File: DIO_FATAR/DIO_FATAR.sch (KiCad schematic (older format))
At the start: 8 parts, among them J1 in, J2 thru

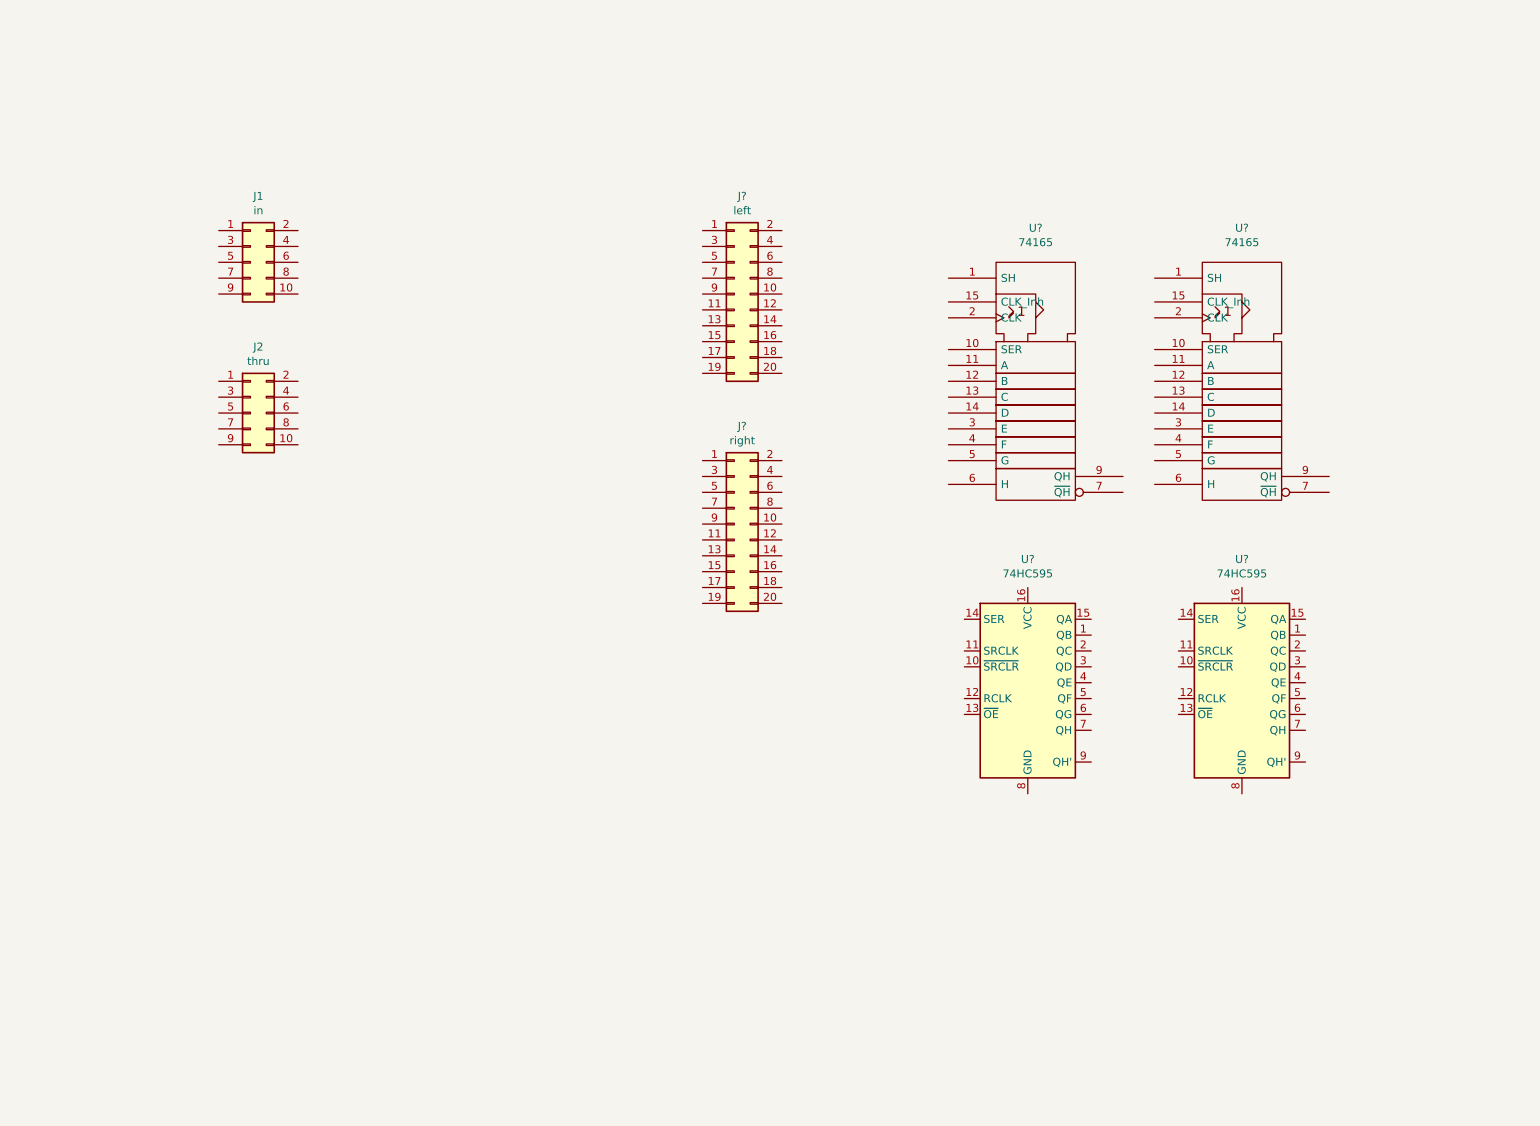
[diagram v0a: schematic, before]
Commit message: DIO_FATAR: schematic mostly done
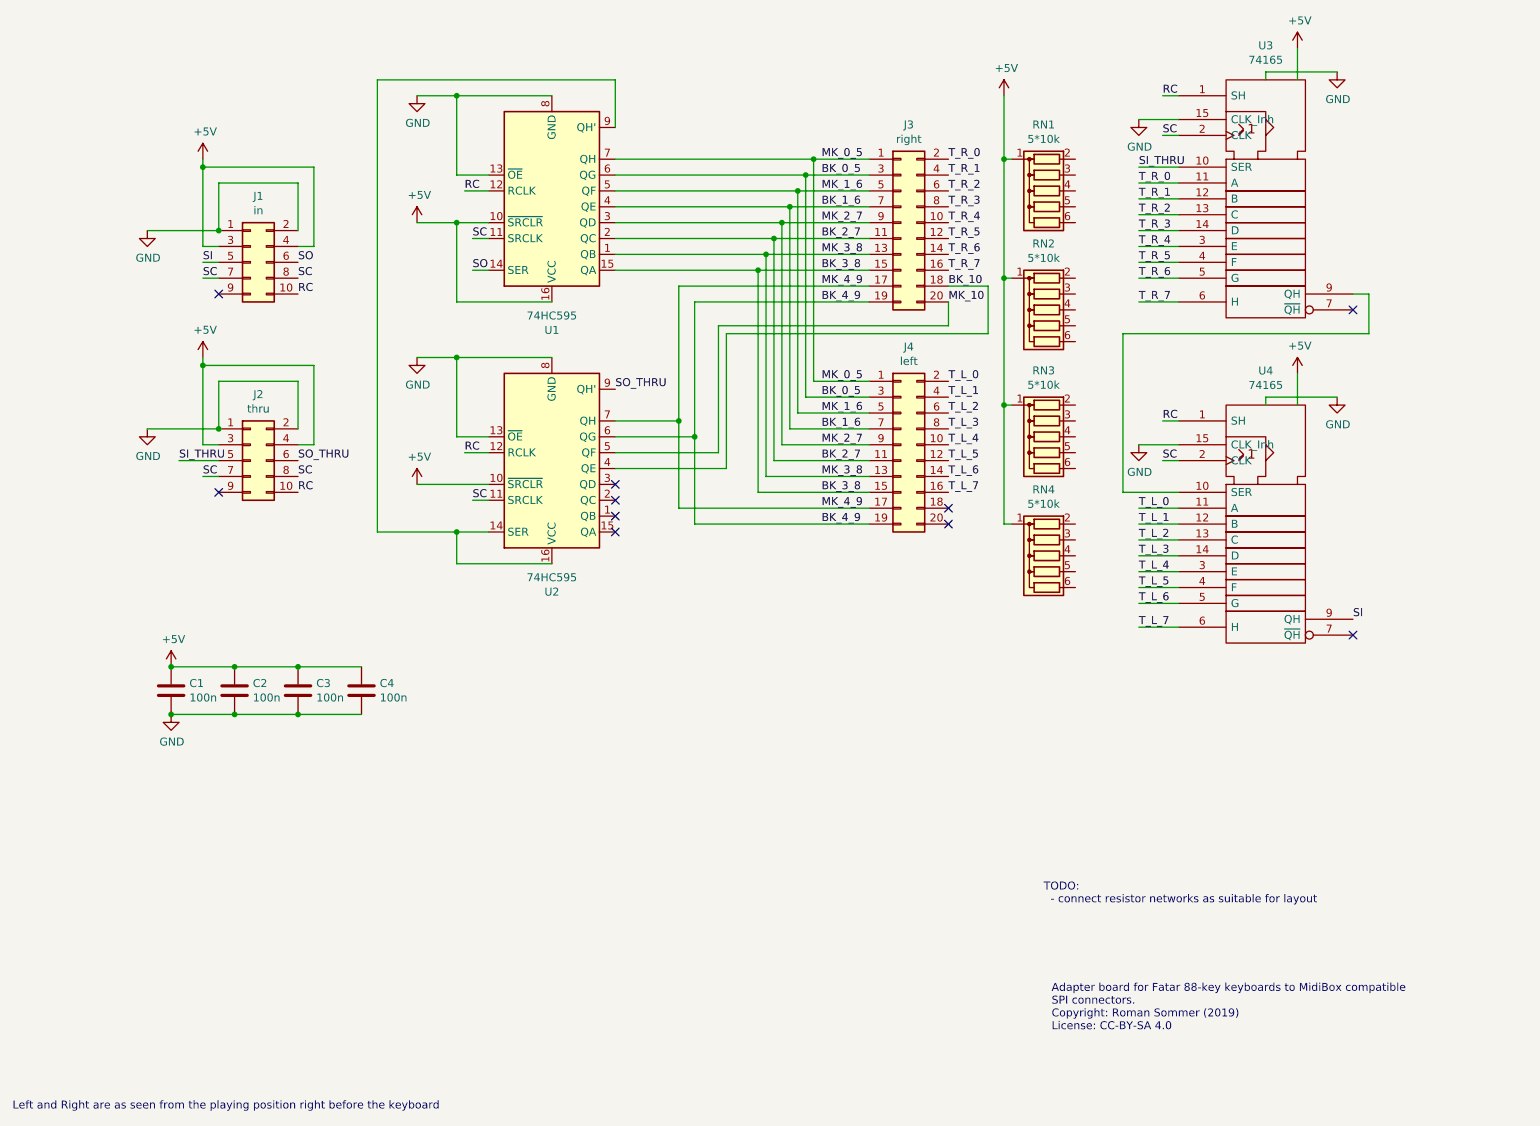
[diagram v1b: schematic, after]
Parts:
- added C1, C2, C3, C4: 100n, symbol Device:C
- added RN1, RN2, RN3, RN4: 5*10k, Resistor_THT:R_Array_SIP6, symbol Device:R_Network05
- gave numbers to parts that had none: 6
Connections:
- net VCC is gone; now on net +5V: U3.16 (VCC), U4.16 (VCC)
- net GND: now also J1.1 (Pin_1), J1.2 (Pin_2), J2.1 (Pin_1), J2.2 (Pin_2), U1.13 (~OE), U1.8 (GND), U2.13 (~OE), U2.8 (GND), U3.15 (CLK_Inh), U4.15 (CLK_Inh), C1.2, C2.2, C3.2, C4.2
- net RC: now reaches J1.10 (Pin_10)
- net RC: now also J2.10 (Pin_10), U1.12 (RCLK), U2.12 (RCLK), U3.1 (SH), U4.1 (SH)
- net +5V: now reaches J1.3 (Pin_3)
- net +5V: now also J1.4 (Pin_4), J2.3 (Pin_3), J2.4 (Pin_4), U1.10 (~SRCLR), U1.16 (VCC), U2.10 (~SRCLR), C1.1, C2.1, C3.1, C4.1, RN1.1 (common), RN2.1 (common), RN3.1 (common), RN4.1 (common)
- net SI: now reaches J1.5 (Pin_5)
- net SI: now also U4.9 (QH)
- net SO: now reaches J1.6 (Pin_6)
- net SO: now also U1.14 (SER)
- net SC: now reaches J1.7 (Pin_7)
- net SC: now also J1.8 (Pin_8), J2.7 (Pin_7), J2.8 (Pin_8), U1.11 (SRCLK), U2.11 (SRCLK), U3.2 (CLK), U4.2 (CLK)
- net MK_0_5: now reaches J4.1 (Pin_1)
- net MK_0_5: now also J3.1 (Pin_1), U1.7 (QH)
- net T_L_4: now reaches J4.10 (Pin_10)
- net T_L_4: now also U4.3 (E)
- net BK_2_7: now reaches J4.11 (Pin_11)
- net BK_2_7: now also J3.11 (Pin_11), U1.2 (QC)
- net T_L_5: now reaches J4.12 (Pin_12)
- net T_L_5: now also U4.4 (F)
- net MK_3_8: now reaches J4.13 (Pin_13)
- net MK_3_8: now also J3.13 (Pin_13), U1.1 (QB)
- net T_L_6: now reaches J4.14 (Pin_14)
- net T_L_6: now also U4.5 (G)
- net BK_3_8: now reaches J4.15 (Pin_15)
- net BK_3_8: now also J3.15 (Pin_15), U1.15 (QA)
- net T_L_7: now reaches J4.16 (Pin_16)
- net T_L_7: now also U4.6 (H)
- net MK_4_9: now reaches J4.17 (Pin_17)
- net MK_4_9: now also J3.17 (Pin_17), U2.7 (QH)
- net BK_4_9: now reaches J4.19 (Pin_19)
- net BK_4_9: now also J3.19 (Pin_19), U2.6 (QG)
- net T_L_0: now reaches J4.2 (Pin_2)
- net T_L_0: now also U4.11 (A)
- net BK_0_5: now reaches J4.3 (Pin_3)
- net BK_0_5: now also J3.3 (Pin_3), U1.6 (QG)
- net T_L_1: now reaches J4.4 (Pin_4)
- net T_L_1: now also U4.12 (B)
- net MK_1_6: now reaches J4.5 (Pin_5)
- net MK_1_6: now also J3.5 (Pin_5), U1.5 (QF)
- net T_L_2: now reaches J4.6 (Pin_6)
- net T_L_2: now also U4.13 (C)
- net BK_1_6: now reaches J4.7 (Pin_7)
- net BK_1_6: now also J3.7 (Pin_7), U1.4 (QE)
- net T_L_3: now reaches J4.8 (Pin_8)
- net T_L_3: now also U4.14 (D)
- net MK_2_7: now reaches J4.9 (Pin_9)
- net MK_2_7: now also J3.9 (Pin_9), U1.3 (QD)
- net T_R_4: now reaches J3.10 (Pin_10)
- net T_R_4: now also U3.3 (E)
- net T_R_5: now reaches J3.12 (Pin_12)
- net T_R_5: now also U3.4 (F)
- net T_R_6: now reaches J3.14 (Pin_14)
- net T_R_6: now also U3.5 (G)
- net T_R_7: now reaches J3.16 (Pin_16)
- net T_R_7: now also U3.6 (H)
- net BK_10: now reaches J3.18 (Pin_18)
- net BK_10: now also U2.4 (QE)
- net T_R_0: now reaches J3.2 (Pin_2)
- net T_R_0: now also U3.11 (A)
- net MK_10: now reaches J3.20 (Pin_20)
- net MK_10: now also U2.5 (QF)
- net T_R_1: now reaches J3.4 (Pin_4)
- net T_R_1: now also U3.12 (B)
- net T_R_2: now reaches J3.6 (Pin_6)
- net T_R_2: now also U3.13 (C)
- net T_R_3: now reaches J3.8 (Pin_8)
- net T_R_3: now also U3.14 (D)
- net SI_THRU: now reaches J2.5 (Pin_5)
- net SI_THRU: now also U3.10 (SER)
- net SO_THRU: now reaches J2.6 (Pin_6)
- net SO_THRU: now also U2.9 (QH')
- net at U4.10 (SER): now also U3.9 (QH)
- net at U1.9 (QH'): now also U2.14 (SER), U2.16 (VCC)
- no-connect marks 0 -> 10
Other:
- note added: "Adapter board for Fatar 88-key keyboards to MidiBox compatible\nSPI connectors.\nCopyright: Roman Sommer (2019)\nLicense: CC-BY-SA 4.0"
- note added: "Left and Right are as seen from the playing position right before the keyboard"
- note added: "TODO:\n - connect resistor networks as suitable for layout\n"
- moved on the sheet: J2, J3, J4, U1, U2, U3, U4

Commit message: DIO_FATAR: add footprint annotations
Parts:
- C1, C2, C3, C4: footprint (none) -> Capacitor_THT:C_Disc_D5.1mm_W3.2mm_P5.00mm
- J1, J2: footprint (none) -> Connector_IDC:IDC-Header_2x05_P2.54mm_Vertical
- J3, J4: footprint (none) -> Connector_IDC:IDC-Header_2x10_P2.54mm_Vertical
- U1, U2, U3, U4: footprint (none) -> Package_DIP:DIP-16_W7.62mm_Socket_LongPads
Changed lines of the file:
@@
 F 0 "J1" H 2200 2567 50  0000 C CNN
 F 1 "in" H 2200 2476 50  0000 C CNN
-F 2 "" H 2150 2150 50  0001 C CNN
+F 2 "Connector_IDC:IDC-Header_2x05_P2.54mm_Vertical" H 2150 2150 50  0001 C CNN
 F 3 "~" H 2150 2150 50  0001 C CNN
 	1    2150 2150
@@
 F 0 "J4" H 6300 3917 50  0000 C CNN
 F 1 "left" H 6300 3826 50  0000 C CNN
-F 2 "" H 6250 3300 50  0001 C CNN
+F 2 "Connector_IDC:IDC-Header_2x10_P2.54mm_Vertical" H 6250 3300 50  0001 C CNN
 F 3 "~" H 6250 3300 50  0001 C CNN
 	1    6250 3300
@@
 F 0 "J3" H 6300 2517 50  0000 C CNN
 F 1 "right" H 6300 2426 50  0000 C CNN
-F 2 "" H 6250 1900 50  0001 C CNN
+F 2 "Connector_IDC:IDC-Header_2x10_P2.54mm_Vertical" H 6250 1900 50  0001 C CNN
 F 3 "~" H 6250 1900 50  0001 C CNN
 	1    6250 1900
@@
 F 0 "J2" H 2200 3817 50  0000 C CNN
 F 1 "thru" H 2200 3726 50  0000 C CNN
-F 2 "" H 2150 3400 50  0001 C CNN
+F 2 "Connector_IDC:IDC-Header_2x05_P2.54mm_Vertical" H 2150 3400 50  0001 C CNN
 F 3 "~" H 2150 3400 50  0001 C CNN
 	1    2150 3400
@@
 F 0 "U4" H 8550 4366 50  0000 C CNN
 F 1 "74165" H 8550 4275 50  0000 C CNN
-F 2 "" H 8550 3600 50  0001 C CNN
+F 2 "Package_DIP:DIP-16_W7.62mm_Socket_LongPads" H 8550 3600 50  0001 C CNN
 F 3 "" H 8550 3600 50  0001 C CNN
 	1    8550 3600
@@
 F 0 "U3" H 8550 2316 50  0000 C CNN
 F 1 "74165" H 8550 2225 50  0000 C CNN
-F 2 "" H 8550 1550 50  0001 C CNN
+F 2 "Package_DIP:DIP-16_W7.62mm_Socket_LongPads" H 8550 1550 50  0001 C CNN
 F 3 "" H 8550 1550 50  0001 C CNN
 	1    8550 1550
@@
 F 0 "U1" H 4050 2578 50  0000 C CNN
 F 1 "74HC595" H 4050 2487 50  0000 C CNN
-F 2 "" H 4050 1800 50  0001 C CNN
+F 2 "Package_DIP:DIP-16_W7.62mm_Socket_LongPads" H 4050 1800 50  0001 C CNN
 F 3 "http://www.ti.com/lit/ds/symlink/sn74hc595.pdf" H 4050 1800 50  0001 C CNN
 	1    4050 1800
@@
 F 0 "U2" H 4050 4228 50  0000 C CNN
 F 1 "74HC595" H 4050 4137 50  0000 C CNN
-F 2 "" H 4050 3450 50  0001 C CNN
+F 2 "Package_DIP:DIP-16_W7.62mm_Socket_LongPads" H 4050 3450 50  0001 C CNN
 F 3 "http://www.ti.com/lit/ds/symlink/sn74hc595.pdf" H 4050 3450 50  0001 C CNN
 	1    4050 3450
@@
 F 0 "C1" H 1765 4896 50  0000 L CNN
 F 1 "100n" H 1765 4805 50  0000 L CNN
-F 2 "" H 1688 4700 50  0001 C CNN
+F 2 "Capacitor_THT:C_Disc_D5.1mm_W3.2mm_P5.00mm" H 1688 4700 50  0001 C CNN
 F 3 "~" H 1650 4850 50  0001 C CNN
 	1    1650 4850
@@
 F 0 "C2" H 2165 4896 50  0000 L CNN
 F 1 "100n" H 2165 4805 50  0000 L CNN
-F 2 "" H 2088 4700 50  0001 C CNN
+F 2 "Capacitor_THT:C_Disc_D5.1mm_W3.2mm_P5.00mm" H 2088 4700 50  0001 C CNN
 F 3 "~" H 2050 4850 50  0001 C CNN
 	1    2050 4850
@@
 F 0 "C3" H 2565 4896 50  0000 L CNN
 F 1 "100n" H 2565 4805 50  0000 L CNN
-F 2 "" H 2488 4700 50  0001 C CNN
+F 2 "Capacitor_THT:C_Disc_D5.1mm_W3.2mm_P5.00mm" H 2488 4700 50  0001 C CNN
 F 3 "~" H 2450 4850 50  0001 C CNN
 	1    2450 4850
@@
 F 0 "C4" H 2965 4896 50  0000 L CNN
 F 1 "100n" H 2965 4805 50  0000 L CNN
-F 2 "" H 2888 4700 50  0001 C CNN
+F 2 "Capacitor_THT:C_Disc_D5.1mm_W3.2mm_P5.00mm" H 2888 4700 50  0001 C CNN
 F 3 "~" H 2850 4850 50  0001 C CNN
 	1    2850 4850

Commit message: DIO_FATAR: use socketless footprint for DIP packages, add netlist
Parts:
- U1, U2, U3, U4: footprint Package_DIP:DIP-16_W7.62mm_Socket_LongPads -> Package_DIP:DIP-16_W7.62mm_LongPads
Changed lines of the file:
@@
 F 0 "U4" H 8550 4366 50  0000 C CNN
 F 1 "74165" H 8550 4275 50  0000 C CNN
-F 2 "Package_DIP:DIP-16_W7.62mm_Socket_LongPads" H 8550 3600 50  0001 C CNN
+F 2 "Package_DIP:DIP-16_W7.62mm_LongPads" H 8550 3600 50  0001 C CNN
 F 3 "" H 8550 3600 50  0001 C CNN
 	1    8550 3600
@@
 F 0 "U3" H 8550 2316 50  0000 C CNN
 F 1 "74165" H 8550 2225 50  0000 C CNN
-F 2 "Package_DIP:DIP-16_W7.62mm_Socket_LongPads" H 8550 1550 50  0001 C CNN
+F 2 "Package_DIP:DIP-16_W7.62mm_LongPads" H 8550 1550 50  0001 C CNN
 F 3 "" H 8550 1550 50  0001 C CNN
 	1    8550 1550
@@
 F 0 "U1" H 4050 2578 50  0000 C CNN
 F 1 "74HC595" H 4050 2487 50  0000 C CNN
-F 2 "Package_DIP:DIP-16_W7.62mm_Socket_LongPads" H 4050 1800 50  0001 C CNN
+F 2 "Package_DIP:DIP-16_W7.62mm_LongPads" H 4050 1800 50  0001 C CNN
 F 3 "http://www.ti.com/lit/ds/symlink/sn74hc595.pdf" H 4050 1800 50  0001 C CNN
 	1    4050 1800
@@
 F 0 "U2" H 4050 4228 50  0000 C CNN
 F 1 "74HC595" H 4050 4137 50  0000 C CNN
-F 2 "Package_DIP:DIP-16_W7.62mm_Socket_LongPads" H 4050 3450 50  0001 C CNN
+F 2 "Package_DIP:DIP-16_W7.62mm_LongPads" H 4050 3450 50  0001 C CNN
 F 3 "http://www.ti.com/lit/ds/symlink/sn74hc595.pdf" H 4050 3450 50  0001 C CNN
 	1    4050 3450
